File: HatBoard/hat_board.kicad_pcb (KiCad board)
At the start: 4 copper layers, 161.5 x 65 mm, 108 parts, among them J1 Molex FC Connection, J11 Molex FC Connection, J12 DF11 FC Connection, J17 Molex FC Connection, J18 DF11 FC Connection, J2 DF11 FC Connection, J23 Molex FC Connection, J24 DF11 FC Connection, J29 Molex FC Connection, J3 Conn_01x04, J30 DF11 FC Connection, J35 Molex FC Connection, J36 DF11 FC Connection, J4 Conn_01x04, J5 Conn_01x04, J6 Conn_01x04, J7 Conn_01x04, J8 Conn_01x04, U1 VEML7700, U10 VEML7700, U12 DRV2605LDGS, U13 TCA4311A, U14 VEML7700, U16 DRV2605LDGS, U17 TCA4311A, U18 VEML7700, U2 DRV2605LDGS, U20 DRV2605LDGS, U21 TCA4311A, U22 VEML7700, U24 DRV2605LDGS, U25 TMP112AIDRLR, U26 TMP112AIDRLR, U27 TMP112AIDRLR, U28 TMP112AIDRLR, U29 TMP112AIDRLR, U30 TMP112AIDRLR, U4 TCA4311A, U5 TCA4311A, U6 VEML7700, U8 DRV2605LDGS, U9 TCA4311A

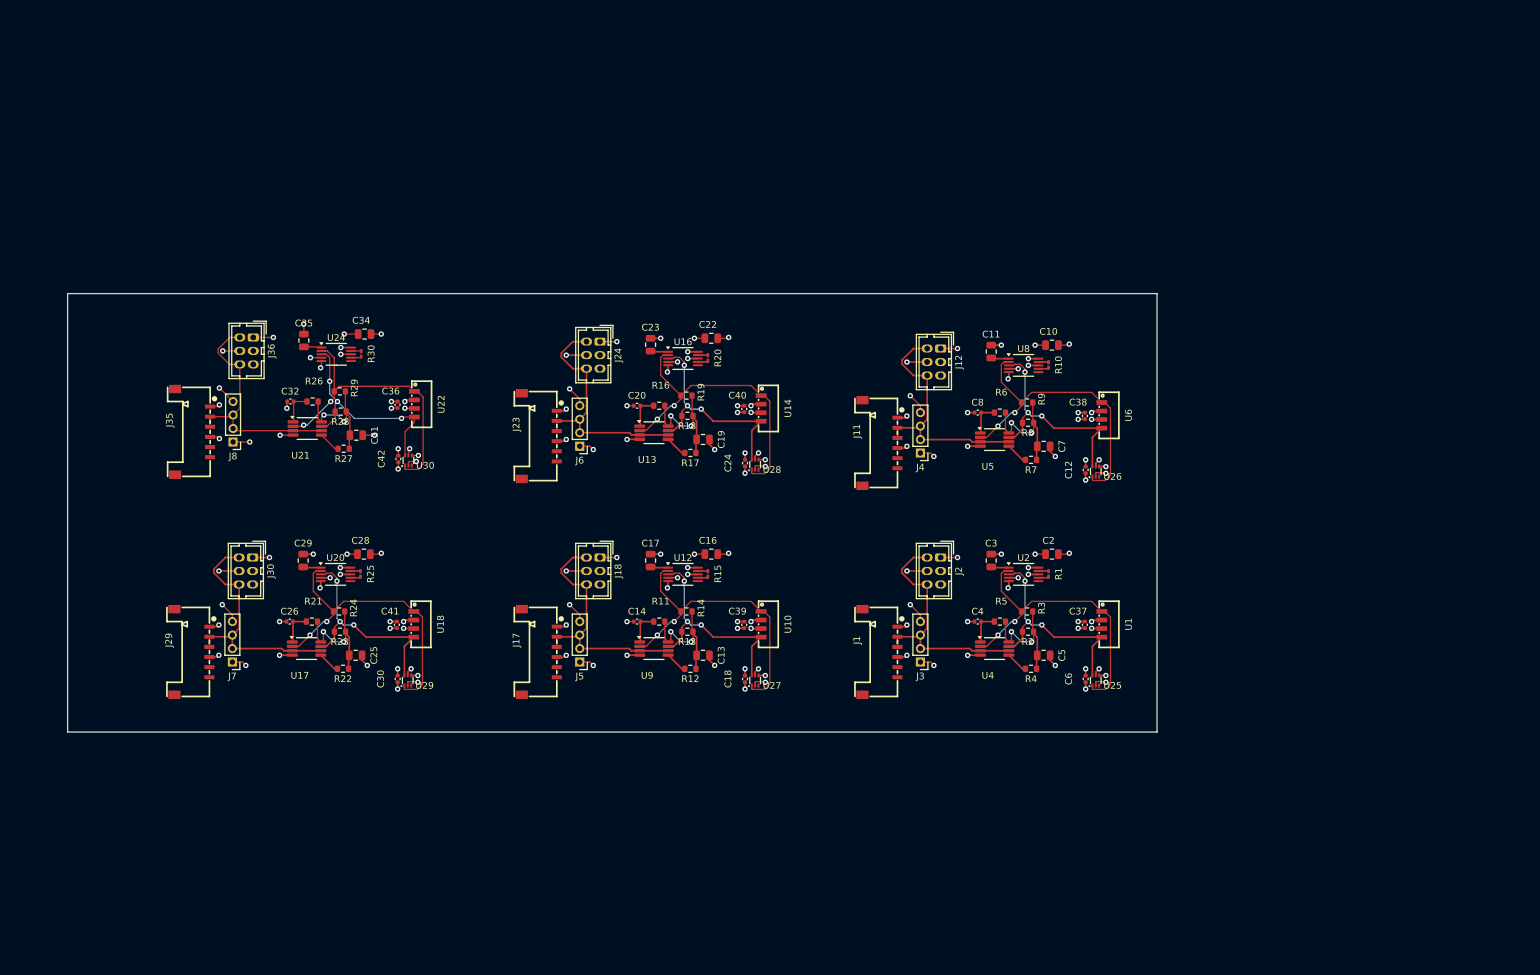
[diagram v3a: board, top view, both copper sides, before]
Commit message: excluded the pad errors
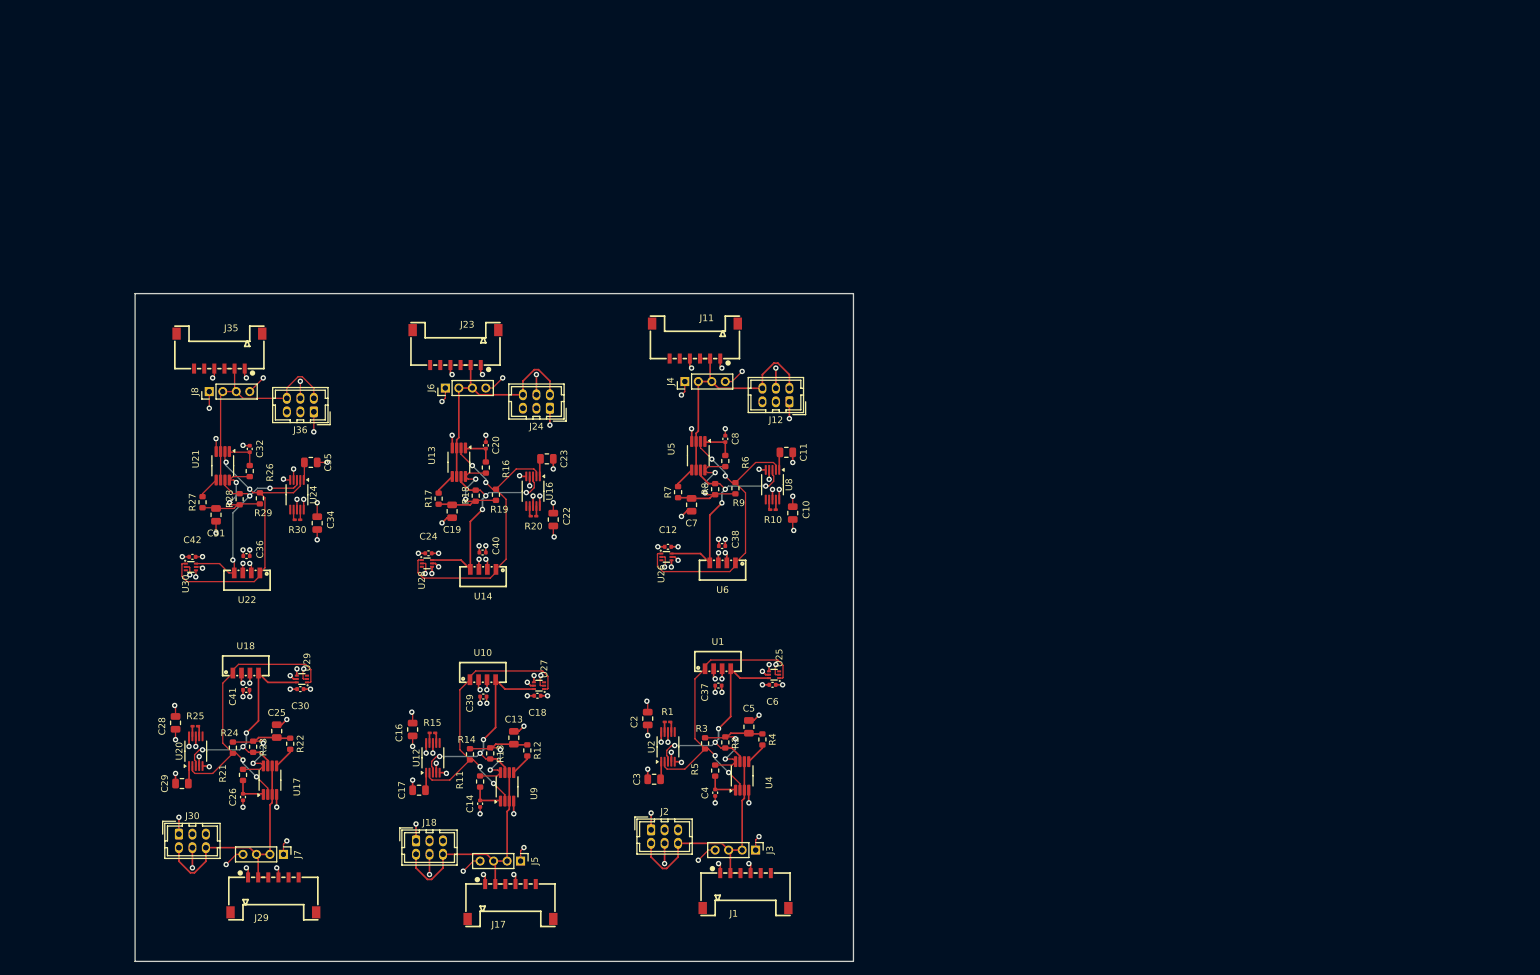
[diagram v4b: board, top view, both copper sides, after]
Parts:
- moved U26 64.9 mm to (129.3, 106.5), turned to 180 degrees
- moved C2 64.7 mm to (126.5, 130.5), turned to 90 degrees
- moved C12 63.0 mm to (129.5, 105.0), turned to 180 degrees
- moved R1 60.6 mm to (129.4, 131.0), turned to 180 degrees
- moved U6 60.3 mm to (137.6, 107.4), turned to 180 degrees
- moved C3 59.6 mm to (127.5, 139.5), turned to 180 degrees
- moved J2 58.9 mm to (127.0, 147.0), turned to 0 degrees
- moved U2 58.6 mm to (129.5, 134.7), turned to 90 degrees
- moved U1 57.3 mm to (136.9, 123.1), turned to 0 degrees
- moved C38 57.1 mm to (137.5, 104.9), turned to 180 degrees
- moved C37 55.1 mm to (137.0, 125.6), turned to 0 degrees
- moved C7 52.9 mm to (133.0, 98.8), turned to -90 degrees
- moved R7 52.5 mm to (131.0, 96.9), turned to 90 degrees
- moved R3 51.6 mm to (135.0, 134.2), turned to -90 degrees
- moved C16 51.3 mm to (91.7, 132.1), turned to 90 degrees
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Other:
- board size 161.5 x 65 mm -> 106.5 x 99 mm

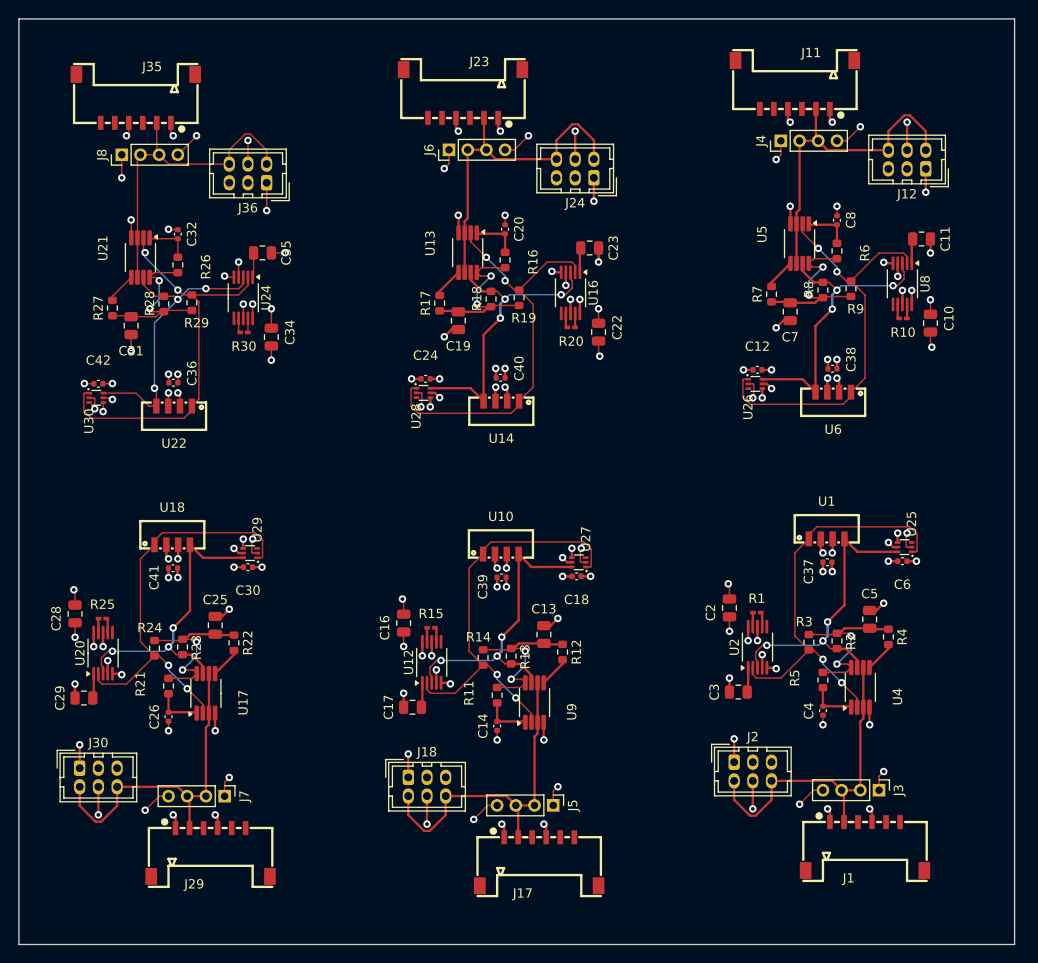
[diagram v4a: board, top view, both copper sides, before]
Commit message: schematic corrections
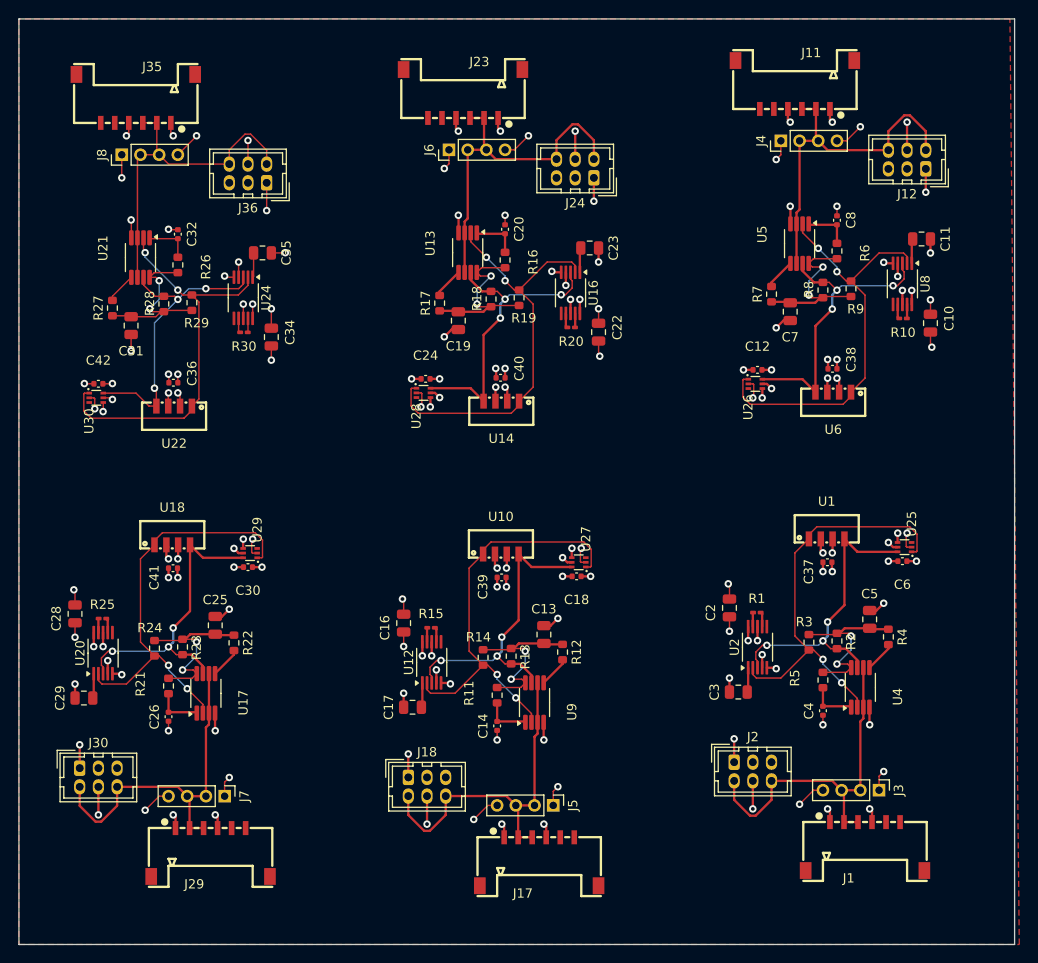
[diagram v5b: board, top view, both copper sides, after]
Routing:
- added copper zone on F.Cu, net GND
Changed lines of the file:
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@@
+	)
+	(zone
+		(net 2)
+		(net_name "GND")
+		(layer "F.Cu")
+		(hatch edge 0.5)
+		(priority 2)
+		(connect_pads
+			(clearance 0)
+		)
+		(min_thickness 0.25)
+		(filled_areas_thickness no)
+		(fill
+			(thermal_gap 0.5)
+			(thermal_bridge_width 0.5)
+		)
+		(polygon
+			(pts
+				(xy 50.5 67.5) (xy 50.5 166.5) (xy 157.5 166.5) (xy 156.5 67.5)
+			)
+		)
 	)
 	(zone

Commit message: updated database
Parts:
- removed C10, C11, C2, C22, C23, C28, C29, C3, C34, C35: 1uF, Capacitor_SMD:C_0805_2012Metric
- removed C12, C24, C30, C36, C6: 100nF, Capacitor_SMD:C_0402_1005Metric
- removed C37, C38, C40, C41, C42: 10nF, Capacitor_SMD:C_0402_1005Metric
- removed J1, J11, J17, J23, J29, J35: Molex FC Connection, easyeda2kicad:CONN-SMD_6P-P1.50_A1501WRB-S-6P
- removed J12, J18, J24, J30, J36: DF11 FC Connection, Connector_Hirose:Hirose_DF11-6DP-2DSA_2x03_P2.00mm_Vertical
- removed J7, J8: Conn_01x04, Connector_PinHeader_2.00mm:PinHeader_1x04_P2.00mm_Vertical
- removed R10, R20, R25, R30: 57.2, Resistor_SMD:R_0201_0603Metric_Pad0.64x0.40mm_HandSolder
- removed R13, R14, R18, R19, R23, R24, R28, R29, R3, R8, R9: 10k, Resistor_SMD:R_0603_1608Metric
- removed U1, U14, U18, U22, U6: VEML7700, easyeda2kicad:SENSOR-SMD_EML7700-TT
- removed U16, U2, U20, U24, U8: DRV2605LDGS, Package_SO:VSSOP-10_3x3mm_P0.5mm
- removed U25, U26, U28, U29, U30: TMP112AIDRLR, easyeda2kicad:SOT-563_L1.6-W1.2-P0.50-LS1.6-BR
- added Cake!: LOGO, LOGO, F.Cu at (195.9, 55.6)
- added D1: D_Schottky, easyeda2kicad:POWERDI-123_L2.8-W1.8-LS3.7-RD, F.Cu at (177.1, 102.6)
- added D2: D_Schottky, easyeda2kicad:POWERDI-123_L2.8-W1.8-LS3.7-RD, F.Cu at (247.0, 50.9)
- added D3: D_Schottky, easyeda2kicad:POWERDI-123_L2.8-W1.8-LS3.7-RD, F.Cu at (239.8, 104.1)
- added D4: D_Schottky, easyeda2kicad:POWERDI-123_L2.8-W1.8-LS3.7-RD, F.Cu at (240.8, 83.2)
- added H1: MountingHole, MountingHole:MountingHole_3.2mm_M3_DIN965_Pad, F.Cu at (169.2, 129.1)
- added H2: MountingHole, MountingHole:MountingHole_3.2mm_M3_DIN965_Pad, F.Cu at (249.2, 129.1)
- J2: value DF11 FC Connection -> Conn_01x04; footprint Connector_Hirose:Hirose_DF11-6DP-2DSA_2x03_P2.00mm_Vertical -> Connector_PinHeader_2.00mm:PinHeader_1x04_P2.00mm_Vertical
- J3, J4, J5, J6: value Conn_01x04 -> DF11 FC Connection; footprint Connector_PinHeader_2.00mm:PinHeader_1x04_P2.00mm_Vertical -> easyeda2kicad:CONN-TH_DF11-12DS-2DSA-05; moved to B.Cu
- R1: value 57.2 -> 10K; footprint Resistor_SMD:R_0201_0603Metric_Pad0.64x0.40mm_HandSolder -> Resistor_SMD:R_0603_1608Metric
- R15: footprint Resistor_SMD:R_0201_0603Metric_Pad0.64x0.40mm_HandSolder -> Resistor_SMD:R_0603_1608Metric
- R2: value 10k -> 10K
- moved R27 183.9 mm to (240.0, 58.7), turned to 180 degrees
- moved C31 181.6 mm to (239.7, 60.8), turned to 180 degrees
- moved U21 176.8 mm to (236.5, 56.3), turned to 0 degrees
- moved C32 172.4 mm to (237.2, 60.1), turned to -90 degrees
- moved R26 170.7 mm to (234.8, 59.8), turned to 0 degrees
- moved J6 148.7 mm to (245.2, 86.3), turned to -90 degrees
- moved J5 146.4 mm to (245.1, 101.3)
- moved R17 145.8 mm to (241.0, 106.8), turned to -90 degrees
- moved R11 143.1 mm to (237.0, 93.4), turned to 180 degrees
- moved C14 139.4 mm to (233.0, 96.5)
- moved U9 138.7 mm to (237.0, 96.1), turned to 0 degrees
- moved U13 138.4 mm to (236.1, 106.9), turned to 0 degrees
- moved R12 138.3 mm to (241.3, 96.3)
- moved C19 137.6 mm to (234.7, 109.9), turned to 180 degrees
- moved C13 133.5 mm to (235.7, 99.2), turned to 180 degrees
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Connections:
- C13 pad 1: Net-(U9-VCC) -> +3V3
- C19 pad 1: Net-(U13-VCC) -> +3V3
- C25 pad 1: Net-(U17-VCC) -> +3V3
- C31 pad 1: Net-(U21-VCC) -> +3V3
- C5 pad 1: Net-(U4-VCC) -> +3V3
- C7 pad 1: Net-(U5-VCC) -> +3V3
- J2 pad 2: /Face Board/SCLIN -> SCL
- J2 pad 3: unconnected-(J2-Pin_3-Pad3) -> SDA
- J2 pad 4: +3V3 -> GND
- J3 pad 1: GND -> unconnected-(J3-Pin_1-Pad1)
- J3 pad 2: /Face Board/SCLIN -> /SDAINZ
- J3 pad 3: /Face Board/SCLIN -> unconnected-(J3-Pin_3-Pad3)
- J3 pad 4: GND -> Net-(D1-K)
- J4 pad 1: GND -> unconnected-(J4-Pin_1-Pad1)
- J4 pad 2: /Face Board1/SCLIN -> unconnected-(J4-Pin_2-Pad2)
- J4 pad 3: /Face Board1/SCLIN -> unconnected-(J4-Pin_3-Pad3)
- J4 pad 4: GND -> unconnected-(J4-Pin_4-Pad4)
- J5 pad 1: GND -> unconnected-(J5-Pin_1-Pad1)
- J5 pad 2: /Face Board2/SCLIN -> /SDAIN_F3
- J5 pad 3: /Face Board2/SCLIN -> unconnected-(J5-Pin_3-Pad3)
- J5 pad 4: GND -> Net-(D3-K)
- J6 pad 1: GND -> unconnected-(J6-Pin_1-Pad1)
- J6 pad 2: /Face Board3/SCLIN -> /SDAIN_F1
- J6 pad 3: /Face Board3/SCLIN -> unconnected-(J6-Pin_3-Pad3)
- J6 pad 4: GND -> Net-(D4-K)
- R1 pad 1: Net-(U2-OUT+) -> SDA
- R1 pad 2: Net-(U2-OUT-) -> +3V3
- R11 pad 1: Net-(U9-VCC) -> +3V3
- R12 pad 1: Net-(U9-VCC) -> +3V3
- R16 pad 1: Net-(U13-VCC) -> +3V3
- R17 pad 1: Net-(U13-VCC) -> +3V3
- R2 pad 1: Net-(U4-VCC) -> SCL
- R2 pad 2: /Face Board/SDA -> +3V3
- R21 pad 1: Net-(U17-VCC) -> +3V3
- R22 pad 1: Net-(U17-VCC) -> +3V3
- R26 pad 1: Net-(U21-VCC) -> +3V3
- R27 pad 1: Net-(U21-VCC) -> +3V3
- R4 pad 1: Net-(U4-VCC) -> +3V3
- R5 pad 1: Net-(U4-VCC) -> +3V3
- R6 pad 1: Net-(U5-VCC) -> +3V3
- R7 pad 1: Net-(U5-VCC) -> +3V3
- U10 pad 1: /Face Board2/SCL -> SCL
- U10 pad 4: /Face Board2/SDA -> SDA
- U12 pad 2: /Face Board2/SCL -> SCL
- U12 pad 3: /Face Board2/SDA -> SDA
- U13 pad 2: /Face Board3/SCL -> SCL
- U13 pad 3: /Face Board3/SCLIN -> /SCLIN_F4
- U13 pad 6: /Face Board3/SCLIN -> /SCDAIN_F4
- U13 pad 7: /Face Board3/SDA -> SDA
- U13 pad 8: Net-(U13-VCC) -> +3V3
- U17 pad 2: /Face Board4/SCL -> SCL
- U17 pad 3: /Face Board4/SCLIN -> /SCLINZ
- U17 pad 6: /Face Board4/SCLIN -> /SDAINZ
- U17 pad 7: /Face Board4/SDA -> SDA
- U17 pad 8: Net-(U17-VCC) -> +3V3
- U21 pad 2: /Face Board5/SCL -> SCL
- U21 pad 3: /Face Board5/SCLIN -> /SDAIN_ANT
- U21 pad 6: /Face Board5/SCLIN -> /SCLIN_ANT
- U21 pad 7: /Face Board5/SDA -> SDA
- U21 pad 8: Net-(U21-VCC) -> +3V3
- U27 pad 1: /Face Board2/SCL -> SCL
- U27 pad 6: /Face Board2/SDA -> SDA
- U4 pad 2: /Face Board/SCL -> SCL
- U4 pad 3: /Face Board/SCLIN -> /SCLIN_F1
- U4 pad 6: /Face Board/SCLIN -> /SDAIN_F1
- U4 pad 7: /Face Board/SDA -> SDA
- U4 pad 8: Net-(U4-VCC) -> +3V3
- U5 pad 2: /Face Board1/SCL -> SCL
- U5 pad 3: /Face Board1/SCLIN -> /SCLIN_F2
- U5 pad 6: /Face Board1/SCLIN -> /SDAIN_F2
- U5 pad 7: /Face Board1/SDA -> SDA
- U5 pad 8: Net-(U5-VCC) -> +3V3
- U9 pad 2: /Face Board2/SCL -> SCL
- U9 pad 3: /Face Board2/SCLIN -> /SCLIN_F3
- U9 pad 6: /Face Board2/SCLIN -> /SDAIN_F3
- U9 pad 7: /Face Board2/SDA -> SDA
- U9 pad 8: Net-(U9-VCC) -> +3V3
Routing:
- net SCL: track 0.00 -> 182.5 mm, vias 0 -> 12
- net SDA: track 0.00 -> 174.0 mm, vias 0 -> 6
- net GND: track 161.2 -> 64.9 mm, vias 96 -> 21
- net /Face Board1/SCL: track 44.9 -> 0.00 mm, vias 2 -> 0
- net /Face Board/SCL: track 44.9 -> 0.00 mm, vias 2 -> 0
- net /Face Board2/SCL: track 44.9 -> 0.00 mm, vias 2 -> 0
- net /Face Board4/SCL: track 44.9 -> 0.00 mm, vias 2 -> 0
- net /Face Board3/SCL: track 44.9 -> 0.00 mm, vias 2 -> 0
- net /Face Board5/SCL: track 43.7 -> 0.00 mm, vias 2 -> 0
- net /Face Board4/SCLIN: track 37.9 -> 0.00 mm
- net /Face Board1/SCLIN: track 37.9 -> 0.00 mm
- net /Face Board/SCLIN: track 37.9 -> 0.00 mm
- net /Face Board3/SCLIN: track 37.9 -> 0.00 mm
- net /Face Board2/SCLIN: track 37.9 -> 0.00 mm
- net /Face Board5/SCLIN: track 36.6 -> 0.00 mm
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- added copper zone on F.Cu, net (none)
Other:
- board size 106.5 x 99 mm -> 88 x 94.5 mm
- board text added: "Antenna Board"
